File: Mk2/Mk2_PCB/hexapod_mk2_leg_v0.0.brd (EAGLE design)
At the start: 27 x 22.4 mm, 5 parts

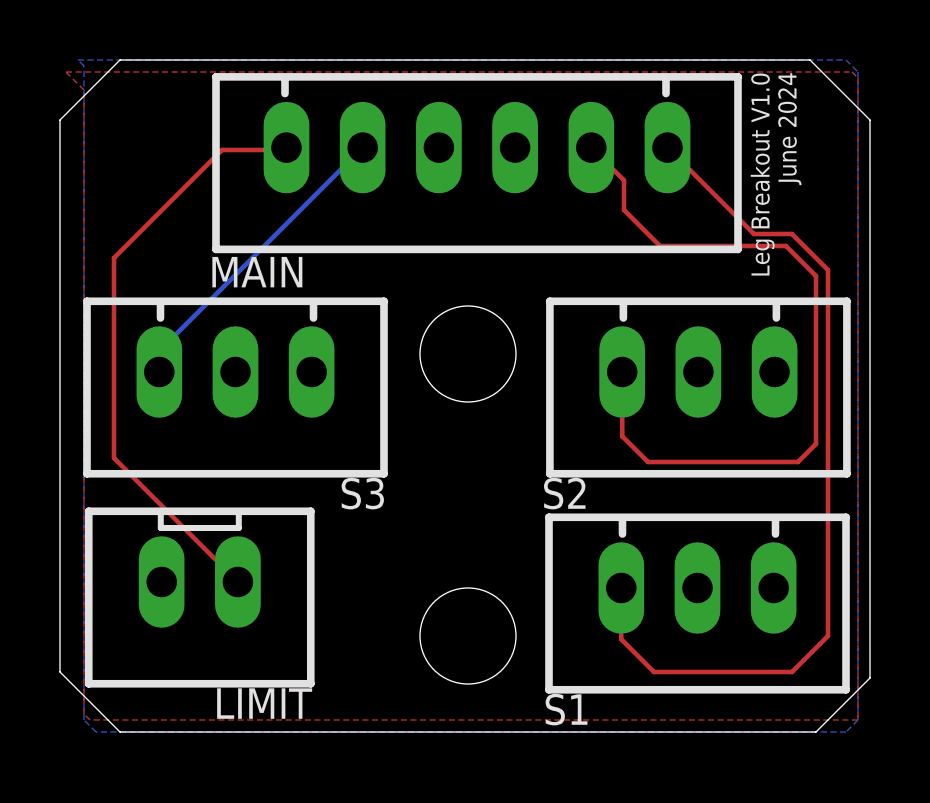
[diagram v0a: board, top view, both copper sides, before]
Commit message: auto route main board. add silkscreens to both
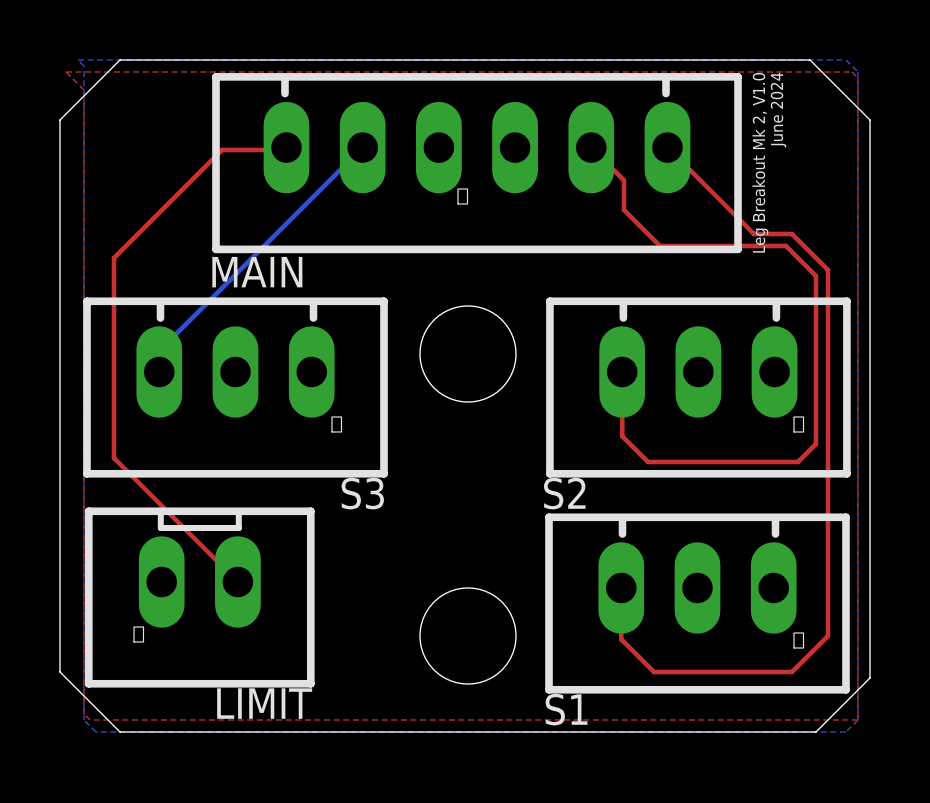
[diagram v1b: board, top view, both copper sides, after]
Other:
- board text added: "Leg Breakout Mk 2, V1.0 June 2024"
- board text added: "⏚"
- board text removed: "Leg Breakout V1.0 June 2024"
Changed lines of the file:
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@@
 <hole x="13.8" y="13.2" drill="3.2"/>
 <hole x="13.8" y="3.8" drill="3.2"/>
-<text x="24" y="22.6" size="0.6" layer="21" rot="R270" align="center-left">Leg Breakout V1.0
+<text x="23.8" y="22.6" size="0.4" layer="21" rot="R270" align="center-left">Leg Breakout Mk 2, V1.0
 June 2024</text>
+<text x="13.4" y="18.2" size="0.5" layer="21">⏚</text>
+<text x="24.6" y="10.6" size="0.5" layer="21">⏚</text>
+<text x="9.2" y="10.6" size="0.5" layer="21">⏚</text>
+<text x="24.6" y="3.4" size="0.5" layer="21">⏚</text>
+<text x="2.6" y="3.6" size="0.5" layer="21">⏚</text>
 </plain>
 <attributes>
@@
 <contactref element="MAIN" pad="6"/>
 <contactref element="LIMIT" pad="1"/>
-<wire x1="6" y1="5.6" x2="6.13" y2="5.6" width="0.1524" layer="16"/>
 <wire x1="7.75" y1="20.08" x2="7.67" y2="20" width="0.1524" layer="1"/>
 <wire x1="2" y1="9.73" x2="6.13" y2="5.6" width="0.1524" layer="1"/>
